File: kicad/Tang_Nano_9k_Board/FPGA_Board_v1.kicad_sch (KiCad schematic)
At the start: 18 parts, among them J1 Conn_01x24, J2 Conn_01x24, J3 Conn_01x08, J4 Conn_01x04, J5 Conn_01x04, J6 Conn_01x04, J7 Conn_01x04, SW1 SW_DIP_x08, SW2 SW_Push, SW3 SW_Push, SW4 SW_Push

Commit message: add led
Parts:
- added D2, D3, D4, D5, D6, D7, D8, D9: IR26-21C_L110_TR8, LED_SMD:LED_1206_3216Metric, symbol LED:IR26-21C_L110_TR8
- added R2, R3, R4, R5, R6, R7, R8, R9: 100, symbol Device:R
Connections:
- net GND: now also J2.23 (Pin_23), U1.26 (GND), D2.1 (K), D3.1 (K), D4.1 (K), D5.1 (K), D6.1 (K), D7.1 (K), D8.1 (K), D9.1 (K)
- net at J1.1 (Pin_1), U1.1 (PIN38): now also R2.1
- net at J1.2 (Pin_2), U1.2 (PIN37): now also R3.1
- net at J1.3 (Pin_3), U1.3 (PIN36): now also R4.1
- net at J1.4 (Pin_4), U1.4 (PIN39): now also R5.1
- net at J1.5 (Pin_5), U1.5 (PIN25): now also R6.1
- net at J1.6 (Pin_6), U1.6 (PIN26): now also R7.1
- net at J1.7 (Pin_7), U1.7 (PIN27): now also R8.1
- net at J1.8 (Pin_8), U1.8 (PIN28): now also R9.1
- net +3V3: now reaches J2.24 (Pin_24), U1.25 (3V3)
- new net: D6.2 (A), R6.2
- new net: D7.2 (A), R7.2
- new net: D8.2 (A), R8.2
- new net: D3.2 (A), R3.2
- new net: D4.2 (A), R4.2
- new net: D9.2 (A), R9.2
- new net: D5.2 (A), R5.2
- new net: D2.2 (A), R2.2
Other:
- moved on the sheet: H1, H2, H3, H4, J3, J4, J5, J6, J7

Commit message: update
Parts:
- removed D2, D3, D4, D5, D6, D7, D8, D9: IR26-21C_L110_TR8, LED_SMD:LED_1206_3216Metric, symbol LED:IR26-21C_L110_TR8
- removed U1: ~, symbol yuma_bf:Tang_Nano_9k
- added Q1, Q2, Q3, Q4, Q5, Q6, Q7, Q8: PMOS, symbol Simulation_SPICE:PMOS
- added R10, R12, R14, R16: 10k, symbol Device:R
- added R11, R13, R15, R17: 1k, symbol Device:R
- added U1: ~, symbol yuma_bf:Tang_Nano_9K
- added U3: TBD62785APG, Package_DIP:DIP-18_W7.62mm, symbol Transistor_Array:TBD62785APG
- added U4: 74HC138, symbol 74xx:74HC138
- R2, R4, R6, R8: value 100 -> 10k
- R3, R5, R7, R9: value 100 -> 1k
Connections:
- net +3V3: now also R2.1, R4.1, R6.1, R8.1, Q1.3 (S), Q2.3 (S), Q3.3 (S), Q4.3 (S), Q5.3 (S), Q6.3 (S), Q7.3 (S), Q8.3 (S), R10.1, R12.1, R14.1, R16.1, U1.25 (3V3), U4.16 (VCC), U4.6 (E2)
- net GND: now also U1.26 (GND), U4.4 (~{E0}), U4.5 (~{E1}), U4.8 (GND)
- net at R6.2: now also R7.1, Q8.2 (G)
- net at R7.2: now also U4.7 (~{Y7})
- net at R8.2: now also R9.1, Q7.2 (G)
- net at J1.2 (Pin_2): now also U1.2 (PIN37), U4.2 (A1); no longer R3.1
- net at R3.2: now also U4.11 (~{Y4})
- net at J1.1 (Pin_1): now also U1.1 (PIN38), U4.1 (A0); no longer R2.1
- net at J1.10 (Pin_10): now also U1.10 (PIN30)
- net at J1.11 (Pin_11): now also U1.11 (PIN33)
- net at J1.12 (Pin_12): now also U1.12 (PIN34)
- net at J1.13 (Pin_13): now also U1.13 (PIN40)
- net at J1.14 (Pin_14): now also U1.14 (PIN35)
- net at J1.15 (Pin_15): now also U1.15 (PIN41)
- net at J1.16 (Pin_16): now also U1.16 (PIN42)
- net at J1.17 (Pin_17): now also U1.17 (PIN51)
- net at J1.18 (Pin_18): now also U1.18 (PIN53)
- net at J1.19 (Pin_19): now also U1.19 (PIN54)
- net at J1.20 (Pin_20): now also U1.20 (PIN55)
- net at J1.21 (Pin_21): now also U1.21 (PIN56)
- net at J1.22 (Pin_22): now also U1.22 (PIN57)
- net at J1.23 (Pin_23): now also U1.23 (HDMI_PIN68)
- net at J1.24 (Pin_24): now also U1.24 (HDMI_PIN69)
- net at J1.3 (Pin_3): now also U1.3 (PIN36), U4.3 (A2); no longer R4.1
- net at J1.4 (Pin_4): now also U1.4 (PIN39); no longer R5.1
- net at J1.5 (Pin_5): now also U1.5 (PIN25); no longer R6.1
- net at J1.6 (Pin_6): now also U1.6 (PIN26); no longer R7.1
- net at J1.7 (Pin_7): now also U1.7 (PIN27); no longer R8.1
- net at J1.8 (Pin_8): now also U1.8 (PIN28); no longer R9.1
- net at J1.9 (Pin_9): now also U1.9 (PIN29)
- net at R4.2: now also R5.1, Q6.2 (G)
- net at J2.2 (Pin_2), SW1.1: now also U1.47 (PIN86)
- net at J2.3 (Pin_3), SW1.2: now also U1.46 (PIN85)
- net at J2.4 (Pin_4), SW1.3: now also U1.45 (PIN84)
- net at J2.5 (Pin_5), SW1.4: now also U1.44 (PIN83)
- net at J2.6 (Pin_6), SW1.5: now also U1.43 (PIN82)
- net at J2.7 (Pin_7), SW1.6: now also U1.42 (PIN81)
- net at J2.8 (Pin_8), SW1.7: now also U1.41 (PIN80)
- net at J2.9 (Pin_9), SW1.8: now also U1.40 (PIN79)
- net at R9.2: now also U4.9 (~{Y6})
- net at J2.22 (Pin_22): now also U1.27 (PIN32)
- net at J2.21 (Pin_21): now also U1.28 (PIN31)
- net at J2.20 (Pin_20): now also U1.29 (PIN49)
- net at J2.19 (Pin_19): now also U1.30 (PIN48)
- net at J2.18 (Pin_18): now also U1.31 (5V)
- net at J2.17 (Pin_17): now also U1.32 (HDMI_PIN70)
- net at J2.16 (Pin_16): now also U1.33 (HDMI_PIN71)
- net at J2.15 (Pin_15): now also U1.34 (HDMI_PIN72)
- net at J2.14 (Pin_14), SW4.1: now also U1.35 (HDMI_PIN73)
- net at J2.13 (Pin_13), SW3.1: now also U1.36 (HDMI_PIN74)
- net at J2.12 (Pin_12), SW2.1: now also U1.37 (HDMI_PIN75)
- net at J2.11 (Pin_11): now also U1.38 (PIN76)
- net at J2.10 (Pin_10): now also U1.39 (PIN77)
- net at J2.1 (Pin_1): now also U1.48 (PIN63)
- net at R5.2: now also U4.10 (~{Y5})
- net at R2.2: now also R3.1, Q5.2 (G)
- new net: Q3.2 (G), R12.2, R13.1
- new net: R13.2, U4.13 (~{Y2})
- new net: Q1.2 (G), R16.2, R17.1
- new net: Q2.2 (G), R14.2, R15.1
- new net: R15.2, U4.14 (~{Y1})
- new net: Q4.2 (G), R10.2, R11.1
- new net: R11.2, U4.12 (~{Y3})
- new net: R17.2, U4.15 (~{Y0})
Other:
- moved on the sheet: H1, H2, H3, H4, J1, J2, J3, J4, J5, J6, J7, SW1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

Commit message: complete FPGA Board tmp
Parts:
- removed D1: IR26-21C_L110_TR8, LED_SMD:LED_1206_3216Metric, symbol LED:IR26-21C_L110_TR8
- removed R1: 120, symbol Device:R
- removed U3: TBD62785APG, Package_DIP:DIP-18_W7.62mm, symbol Transistor_Array:TBD62785APG
- added R18, R19, R20, R21, R22, R23, R24, R25: 600, symbol Device:R
- added U2: ~, symbol yuma_bf:OSL641501-BRA
- added U3: TBD62083AFG, Package_DIP:DIP-18_W7.62mm, symbol yuma_bf:TBD62083AFG
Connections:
- net GND: now also U3.10 (GND)
- net at Q3.1 (D): now also U2. (R8)
- net C7: now reaches J1.10 (Pin_10), U1.10 (PIN30)
- net C7: now also U3.12 (O7)
- net C8: now reaches J1.11 (Pin_11), U1.11 (PIN33)
- net C8: now also U3.11 (O8)
- net C1: now reaches J1.4 (Pin_4), U1.4 (PIN39)
- net C1: now also U3.18 (O1)
- net C2: now reaches J1.5 (Pin_5), U1.5 (PIN25)
- net C2: now also U3.17 (O2)
- net C3: now reaches J1.6 (Pin_6), U1.6 (PIN26)
- net C3: now also U3.16 (O3)
- net C4: now reaches J1.7 (Pin_7), U1.7 (PIN27)
- net C4: now also U3.15 (O4)
- net C5: now reaches J1.8 (Pin_8), U1.8 (PIN28)
- net C5: now also U3.14 (O5)
- net C6: now reaches J1.9 (Pin_9), U1.9 (PIN29)
- net C6: now also U3.13 (O6)
- net at Q1.1 (D): now also U2. (R8)
- net at Q6.1 (D): now also U2. (R8)
- net at Q4.1 (D): now also U2. (R8)
- net at Q7.1 (D): now also U2. (R8)
- net at Q8.1 (D): now also U2. (R8)
- net at Q5.1 (D): now also U2. (R8)
- net at Q2.1 (D): now also U2. (R8)
- new net: R19.1, U2. (R8)
- new net: R25.1, U2. (R8)
- new net: R18.1, U2. (R8)
- new net: R24.1, U2. (R8)
- new net: R21.1, U2. (R8)
- new net: R20.1, U2. (R8)
- new net: R23.1, U2. (R8)
- new net: R22.1, U2. (R8)
- new net: R19.2, U3.2 (I2)
- new net: R25.2, U3.8 (I8)
- new net: R18.2, U3.1 (I1)
- new net: R20.2, U3.3 (I3)
- new net: R21.2, U3.4 (I4)
- new net: R22.2, U3.5 (I5)
- new net: R23.2, U3.6 (I6)
- new net: R24.2, U3.7 (I7)
- no-connect marks 0 -> 1
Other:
- moved on the sheet: J4, J5, J6, J7

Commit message: set footprint
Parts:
- removed Q1, Q2, Q3, Q4, Q5, Q6, Q7, Q8: PMOS, symbol Simulation_SPICE:PMOS
- removed R10, R12, R14, R16, R2, R4, R6, R8: 10k, symbol Device:R
- removed R11, R13, R15, R17, R3, R5, R7, R9: 1k, symbol Device:R
- added U5: TBD62783A, Package_DIP:DIP-18_W7.62mm, symbol Transistor_Array:TBD62783A
- H1, H2, H3, H4: footprint (none) -> MountingHole:MountingHole_2.1mm
- J1, J2: footprint (none) -> Connector_PinHeader_2.54mm:PinHeader_1x24_P2.54mm_Vertical
- J3: footprint (none) -> Connector_PinHeader_2.54mm:PinHeader_1x08_P2.54mm_Vertical
- J4, J5, J6, J7: footprint (none) -> Connector_PinHeader_2.54mm:PinHeader_1x04_P2.54mm_Vertical
- R18, R19, R20, R21, R22, R23, R24, R25: footprint (none) -> Resistor_THT:R_Axial_DIN0207_L6.3mm_D2.5mm_P7.62mm_Horizontal
- SW1: footprint (none) -> Button_Switch_THT:SW_DIP_SPSTx07_Slide_9.78x19.96mm_W7.62mm_P2.54mm
- SW2, SW3, SW4: footprint (none) -> Button_Switch_SMD:Panasonic_EVQPUJ_EVQPUA
- U1: footprint (none) -> BFP:Tang_Nano_9K
- U2: footprint (none) -> BFP:OSL641501-BX
- U4: footprint (none) -> Package_DIP:CERDIP-16_W7.62mm_SideBrazed
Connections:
- net +3V3: now also U5.9 (VCC)
- net GND: now also U5.10 (GND)
- net at U2. (R8): now also U5.18 (O1)
- net at U4.13 (~{Y2}): now also U5.3 (I3)
- net at U4.14 (~{Y1}): now also U5.2 (I2)
- net at U4.10 (~{Y5}): now also U5.6 (I6)
- net at U4.11 (~{Y4}): now also U5.5 (I5)
- net at U4.12 (~{Y3}): now also U5.4 (I4)
- net at U4.15 (~{Y0}): now also U5.1 (I1)
- net at U4.7 (~{Y7}): now also U5.8 (I8)
- net at U4.9 (~{Y6}): now also U5.7 (I7)
- new net: U2. (R8), U5.11 (O8)
- new net: U2. (R8), U5.12 (O7)
- new net: U2. (R8), U5.13 (O6)
- new net: U2. (R8), U5.14 (O5)
- new net: U2. (R8), U5.15 (O4)
- new net: U2. (R8), U5.16 (O3)
- new net: U2. (R8), U5.17 (O2)

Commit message: making pcb board
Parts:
- R18, R19, R20, R21, R22, R23, R24, R25: value 600 -> 750
- SW1: footprint Button_Switch_THT:SW_DIP_SPSTx07_Slide_9.78x19.96mm_W7.62mm_P2.54mm -> Button_Switch_THT:SW_DIP_SPSTx08_Slide_9.78x22.5mm_W7.62mm_P2.54mm
- U1: footprint BFP:Tang_Nano_9K -> BFP_footprints:Tang_Nano_9K
- U2: footprint BFP:OSL641501-BX -> BFP_footprints:OSL641501-BX
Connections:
- net at R19.1: now also U2.3 (C2); no longer U2. (R8)
- net at R25.1: now also U2.16 (C8); no longer U2. (R8)
- net at R18.1: now also U2.13 (C1); no longer U2. (R8)
- net at R24.1: now also U2.15 (C7); no longer U2. (R8)
- net at R21.1: now also U2.10 (C4); no longer U2. (R8)
- net at R20.1: now also U2.4 (C3); no longer U2. (R8)
- net at R23.1: now also U2.11 (C6); no longer U2. (R8)
- net at R22.1: now also U2.6 (C5); no longer U2. (R8)
- net at U5.11 (O8): now also U2.5 (R8); no longer U2. (R8)
- net at U5.12 (O7): now also U2.2 (R7); no longer U2. (R8)
- net at U5.13 (O6): now also U2.7 (R6); no longer U2. (R8)
- net at U5.14 (O5): now also U2.1 (R5); no longer U2. (R8)
- net at U5.15 (O4): now also U2.12 (R4); no longer U2. (R8)
- net at U5.16 (O3): now also U2.8 (R3); no longer U2. (R8)
- net at U5.17 (O2): now also U2.14 (R2); no longer U2. (R8)
- net at U5.18 (O1): now also U2.9 (R1); no longer U2. (R8)

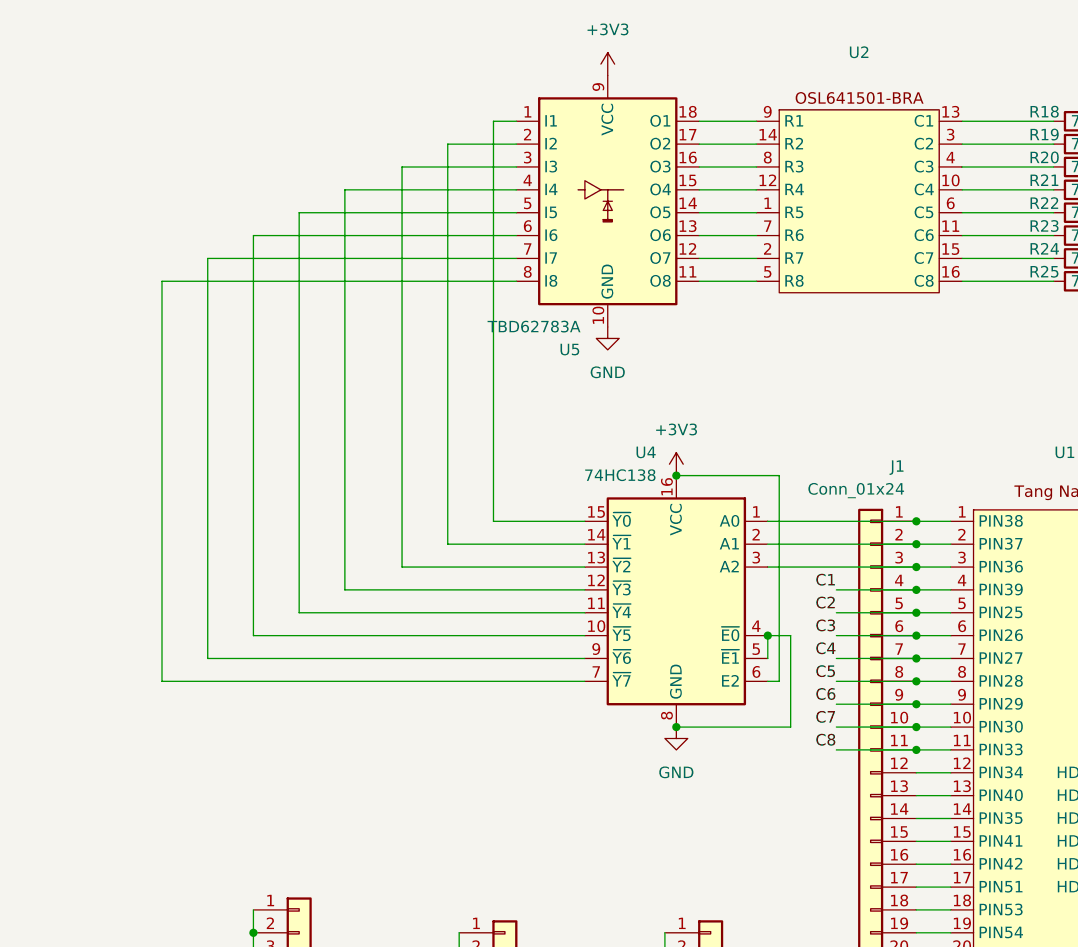
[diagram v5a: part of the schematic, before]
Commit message: set pcb position
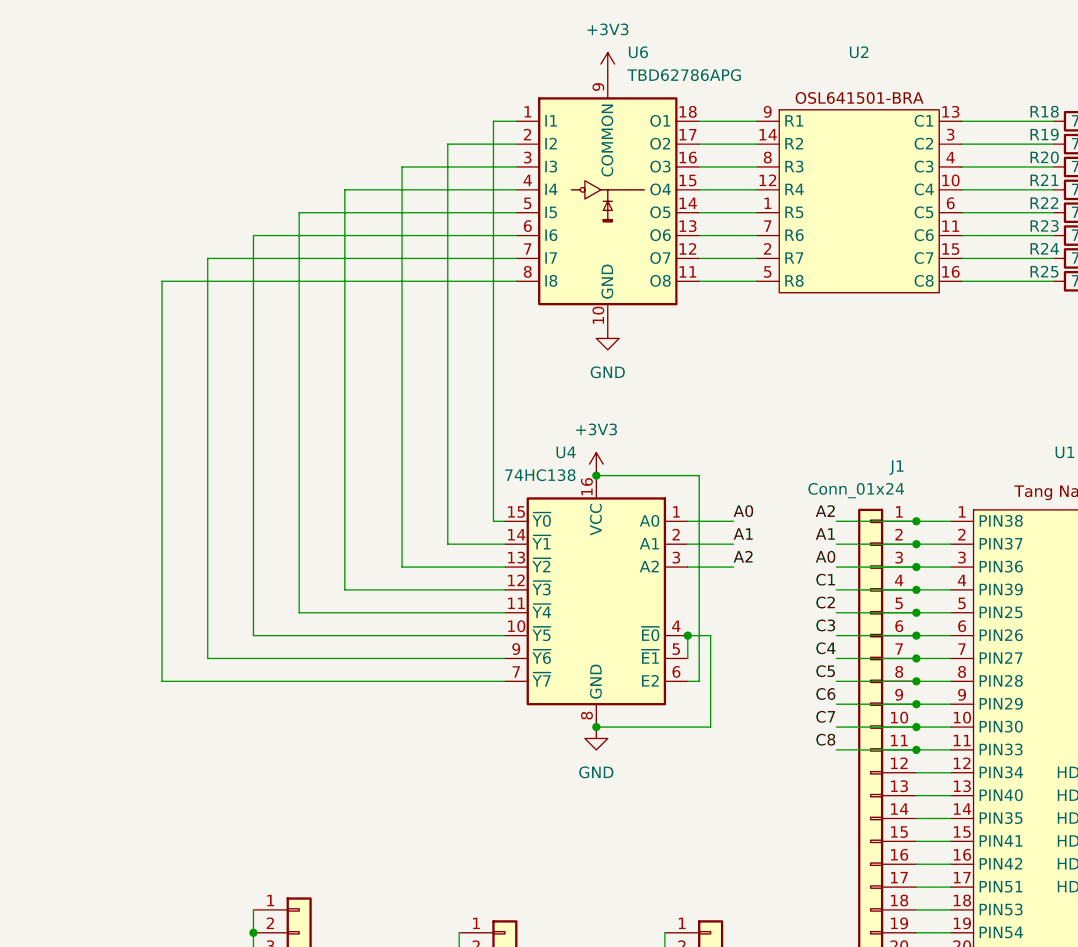
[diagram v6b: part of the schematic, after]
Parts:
- removed U5: TBD62783A, Package_DIP:DIP-18_W7.62mm, symbol Transistor_Array:TBD62783A
- added U6: TBD62786APG, Package_DIP:DIP-18_W7.62mm, symbol yuma_bf:TBD62786APG
- H1, H2, H3, H4: footprint MountingHole:MountingHole_2.1mm -> MountingHole:MountingHole_3.2mm_M3
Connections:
- net +3V3: now also U6.9 (COMMON)
- net GND: now also U6.10 (GND)
- net at U2.1 (R5): now also U6.14 (O5)
- net at U2.12 (R4): now also U6.15 (O4)
- net at U2.14 (R2): now also U6.17 (O2)
- net at U2.2 (R7): now also U6.12 (O7)
- net at U2.5 (R8): now also U6.11 (O8)
- net at U2.7 (R6): now also U6.13 (O6)
- net at U2.8 (R3): now also U6.16 (O3)
- net at U2.9 (R1): now also U6.18 (O1)
- net A2: now reaches J1.1 (Pin_1), U1.1 (PIN38)
- net A2: now also U4.3 (A2); no longer U4.1 (A0)
- net A1: now reaches J1.2 (Pin_2), U1.2 (PIN37), U4.2 (A1)
- net A0: now reaches J1.3 (Pin_3), U1.3 (PIN36)
- net A0: now also U4.1 (A0); no longer U4.3 (A2)
- net at U4.10 (~{Y5}): now also U6.6 (I6)
- net at U4.11 (~{Y4}): now also U6.5 (I5)
- net at U4.12 (~{Y3}): now also U6.4 (I4)
- net at U4.13 (~{Y2}): now also U6.3 (I3)
- net at U4.14 (~{Y1}): now also U6.2 (I2)
- net at U4.15 (~{Y0}): now also U6.1 (I1)
- net at U4.7 (~{Y7}): now also U6.8 (I8)
- net at U4.9 (~{Y6}): now also U6.7 (I7)
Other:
- moved on the sheet: U4
